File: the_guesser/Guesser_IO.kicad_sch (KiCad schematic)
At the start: 17 parts, among them J1 Screw_Terminal_01x06, J4 Screw_Terminal_01x06, J7 USB_C_Receptacle_USB2.0_16P, Q1 AS2312, Q2 AS2312, Q3 AS2312, Q4 AS2312, Q5 AS2312, Q6 AS2312, U13 TPD4S014DSQR, U60 FUSB307BMPX

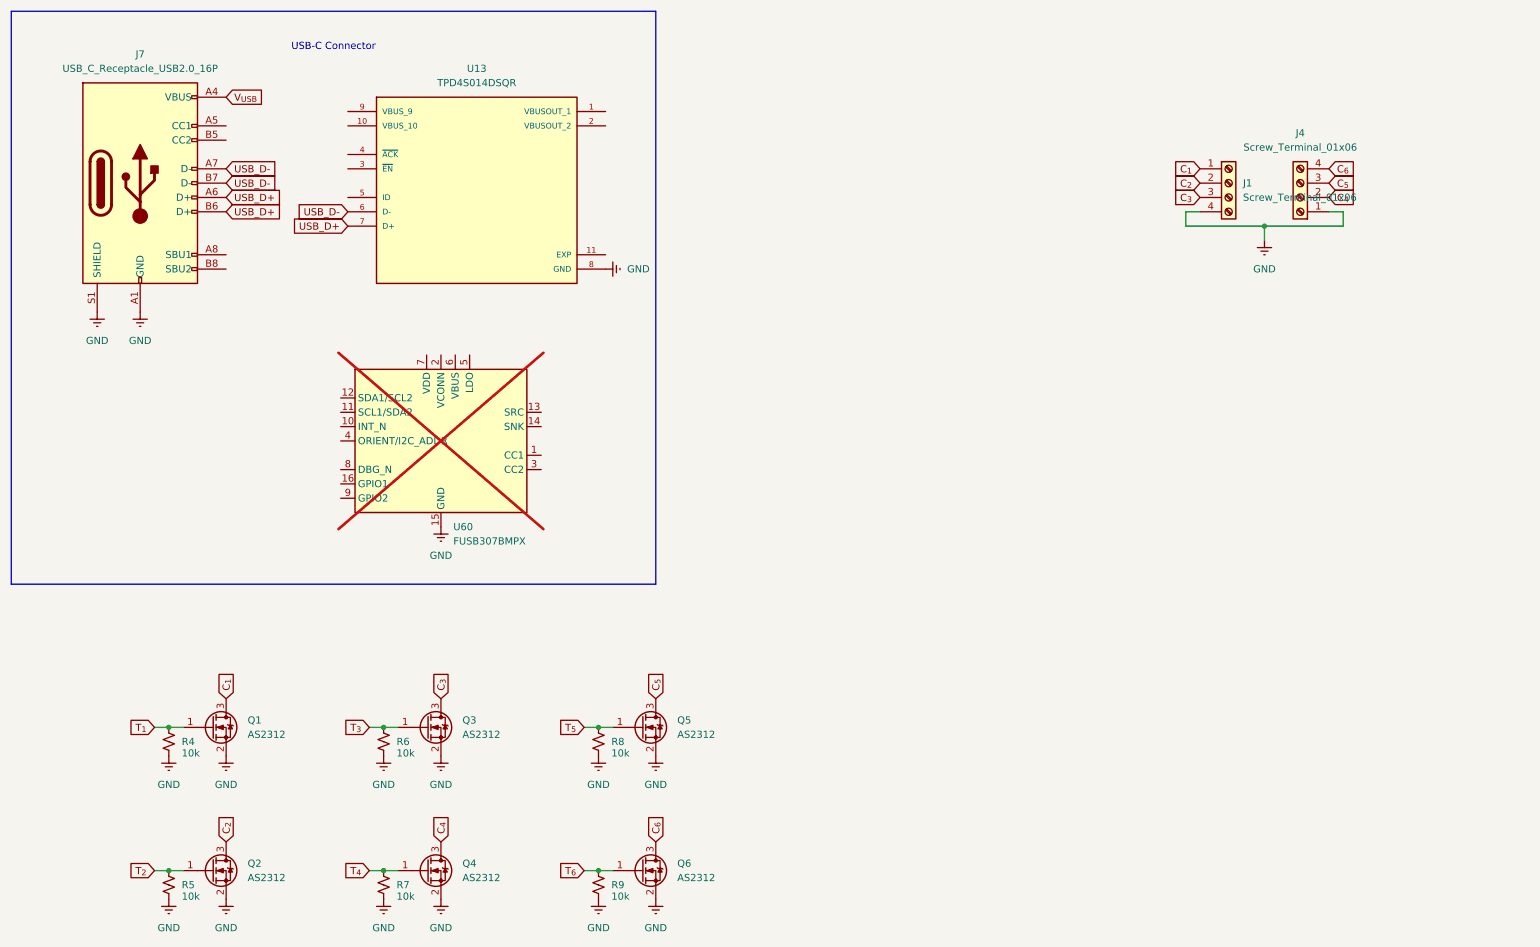
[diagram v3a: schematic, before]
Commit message: Finished routing Guesser
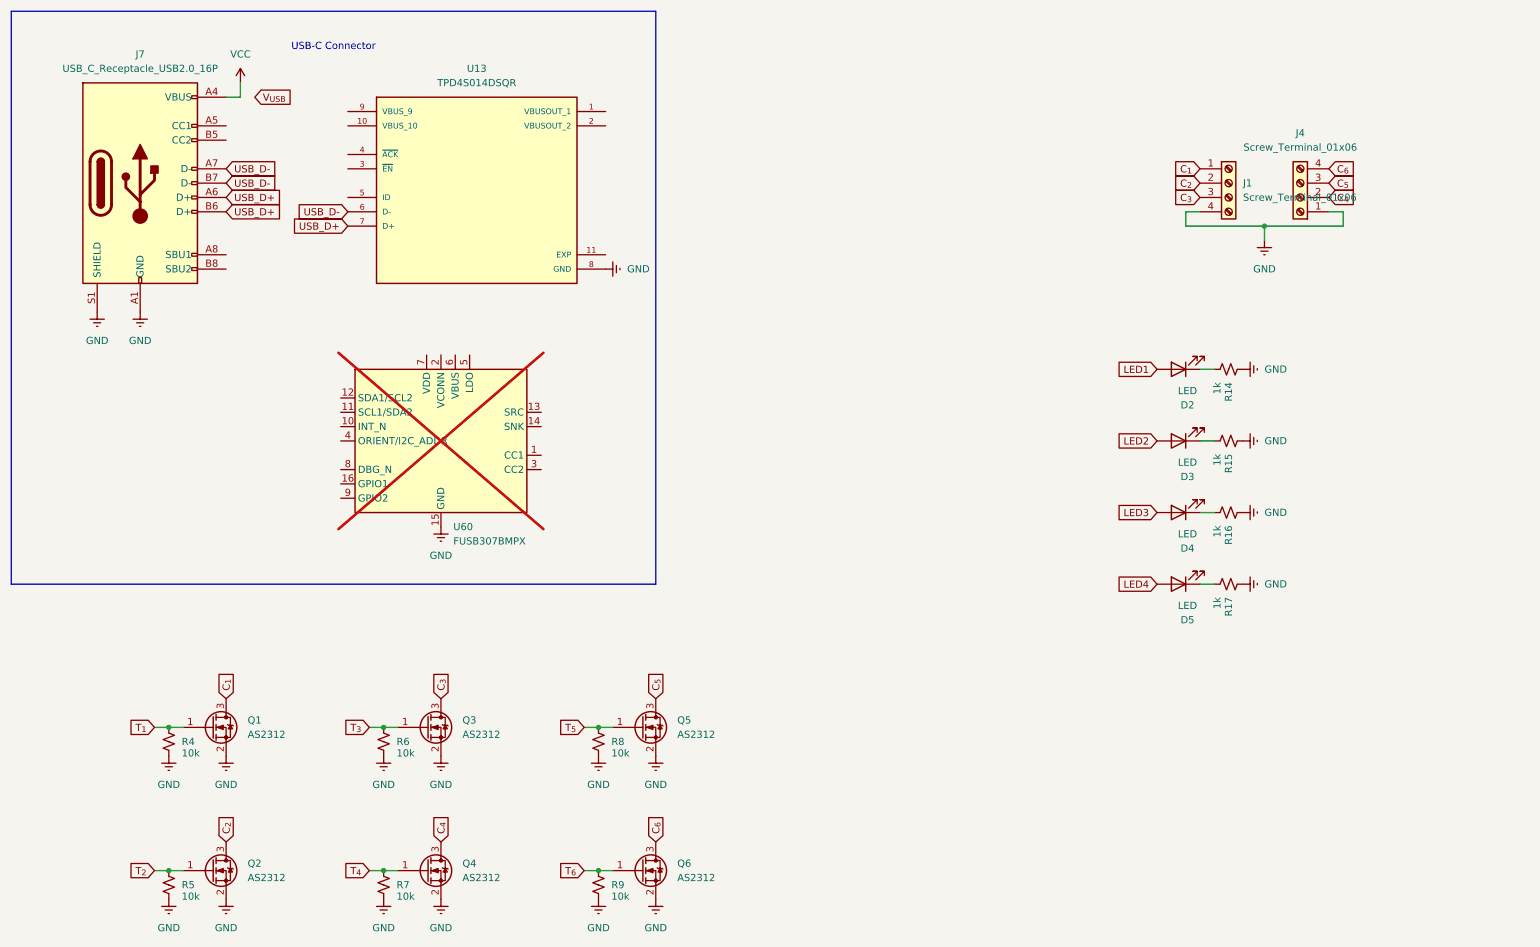
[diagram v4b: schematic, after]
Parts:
- added D2, D3, D4, D5: LED, LED_SMD:LED_0603_1608Metric, symbol Device:LED
- added R14, R15, R16, R17: 1k, Resistor_SMD:R_0603_1608Metric, symbol Device:R_Small_US
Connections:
- net GND: now also R14.1, R15.1, R16.1, R17.1
- net V_{USB}: no longer J7.A4 (VBUS), J7.A9 (VBUS), J7.B4 (VBUS), J7.B9 (VBUS)
- new net: D4.1 (K), R16.2
- new net: D3.1 (K), R15.2
- new net: D2.1 (K), R14.2
- new net: D5.1 (K), R17.2
- new net LED1: D2.2 (A)
- new net LED2: D3.2 (A)
- new net LED3: D4.2 (A)
- new net LED4: D5.2 (A)
- new net VCC: J7.A4 (VBUS), J7.A9 (VBUS), J7.B4 (VBUS), J7.B9 (VBUS)

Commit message: Started Timer Programmer
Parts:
- removed J7: USB_C_Receptacle_USB2.0_16P, Connector_USB:USB_C_Receptacle_GCT_USB4110, symbol Connector:USB_C_Receptacle_USB2.0_16P
- added J5: R41-B583A, locals_but_working_PLEASE:CONN_R41-B583A_MIT, symbol Connector:USB_C_Receptacle
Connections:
- net GND: now also J5.A1 (GND), J5.A12 (GND), J5.B1 (GND), J5.B12 (GND), J5.S1 (SHIELD)
- net USB_D+: now also J5.A6 (D+), J5.B6 (D+)
- net USB_D-: now also J5.A7 (D-), J5.B7 (D-)
- net VCC: now also J5.A4 (VBUS), J5.A9 (VBUS), J5.B4 (VBUS), J5.B9 (VBUS)
- no-connect marks 0 -> 8
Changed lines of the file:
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@@
 		(color 0 0 0 0)
 	)
+	(no_connect
+		(at 50.8 60.96)
+	)
+	(no_connect
+		(at 50.8 76.2)
+	)
+	(no_connect
+		(at 50.8 55.88)
+	)
+	(no_connect
+		(at 50.8 78.74)
+	)
+	(no_connect
+		(at 50.8 68.58)
+	)
+	(no_connect
+		(at 50.8 71.12)
+	)
+	(no_connect
+		(at 50.8 63.5)
+	)
+	(no_connect
+		(at 50.8 53.34)
+	)
 	(wire
 		(pts
@@
 		)
 	)
-	(global_label "V_{USB}"
-		(shape input)
-		(at 55.88 27.94 0)
-		(fields_autoplaced yes)
-		(effects
-			(font
-				(size 1.27 1.27)
-			)
-			(justify left)
-		)
-		(property "Intersheetrefs" "${INTERSHEET_REFS}"
-			(at 63.0526 27.94 0)
-			(effects
-				(font
-					(size 1.27 1.27)
-				)
-				(justify left)
-				(hide yes)
-			)
-		)
-	)
 	(global_label "C_{4}"
 		(shape input)
@@
 	(symbol
 		(lib_id "power:Earth")
-		(at 27.94 66.04 0)
+		(at 27.94 93.98 0)
 		(unit 1)
 		(exclude_from_sim no)
@@
 		(fields_autoplaced yes)
 		(property "Reference" "#PWR045"
-			(at 27.94 72.39 0)
+			(at 27.94 100.33 0)
 			(effects
 				(font
@@
 		)
 		(property "Value" "GND"
-			(at 27.94 71.12 0)
+			(at 27.94 99.06 0)
 			(effects
 				(font
@@
 		)
 		(property "Footprint" ""
-			(at 27.94 66.04 0)
+			(at 27.94 93.98 0)
 			(effects
 				(font
@@
 		)
 		(property "Datasheet" "~"
-			(at 27.94 66.04 0)
+			(at 27.94 93.98 0)
 			(effects
 				(font
@@
 		)
 		(property "Description" "Power symbol creates a global label with name \"Earth\""
-			(at 27.94 66.04 0)
+			(at 27.94 93.98 0)
 			(effects
 				(font
@@
 	)
 	(symbol
-		(lib_id "Connector:USB_C_Receptacle_USB2.0_16P")
-		(at 35.56 43.18 0)
-		(unit 1)
-		(exclude_from_sim no)
-		(in_bom yes)
-		(on_board yes)
-		(dnp no)
-		(fields_autoplaced yes)
-		(property "Reference" "J7"
-			(at 35.56 20.32 0)
-			(effects
-				(font
-					(size 1.27 1.27)
-				)
-			)
-		)
-		(property "Value" "USB_C_Receptacle_USB2.0_16P"
-			(at 35.56 22.86 0)
-			(effects
-				(font
-					(size 1.27 1.27)
-				)
-			)
-		)
-		(property "Footprint" "Connector_USB:USB_C_Receptacle_GCT_USB4110"
-			(at 39.37 43.18 0)
-			(effects
-				(font
-					(size 1.27 1.27)
-				)
-				(hide yes)
-			)
-		)
-		(property "Datasheet" "https://www.usb.org/sites/default/files/documents/usb_type-c.zip"
-			(at 39.37 43.18 0)
-			(effects
-				(font
-					(size 1.27 1.27)
-				)
-				(hide yes)
-			)
-		)
-		(property "Description" "USB 2.0-only 16P Type-C Receptacle connector"
-			(at 35.56 43.18 0)
-			(effects
-				(font
-					(size 1.27 1.27)
-				)
-				(hide yes)
-			)
-		)
-		(pin "B12"
-		)
-		(pin "A5"
-		)
-		(pin "B7"
-		)
-		(pin "A7"
-		)
-		(pin "B8"
-		)
-		(pin "A12"
-		)
-		(pin "S1"
-		)
-		(pin "B1"
-		)
-		(pin "B6"
-		)
-		(pin "B5"
-		)
-		(pin "A9"
-		)
-		(pin "A1"
-		)
-		(pin "A6"
-		)
-		(pin "A8"
-		)
-		(pin "A4"
-		)
-		(pin "B4"
-		)
-		(pin "B9"
-		)
-		(instances
-			(project "the_guesser"
-				(path "/473e3a2e-6c5e-4995-af4a-e4bf1449cab0/0bcaec57-f6d5-41f0-b678-342e153337b7"
-					(reference "J7")
-					(unit 1)
-				)
-			)
-		)
-	)
-	(symbol
 		(lib_id "Connector:Screw_Terminal_01x04")
 		(at 228.6 43.18 0)
@@
 	)
 	(symbol
+		(lib_id "Connector:USB_C_Receptacle")
+		(at 35.56 53.34 0)
+		(unit 1)
+		(exclude_from_sim no)
+		(in_bom yes)
+		(on_board yes)
+		(dnp no)
+		(fields_autoplaced yes)
+		(property "Reference" "J5"
+			(at 35.56 20.32 0)
+			(effects
+				(font
+					(size 1.27 1.27)
+				)
+			)
+		)
+		(property "Value" "R41-B583A"
+			(at 35.56 22.86 0)
+			(effects
+				(font
+					(size 1.27 1.27)
+				)
+			)
+		)
+		(property "Footprint" "locals_but_working_PLEASE:CONN_R41-B583A_MIT"
+			(at 39.37 53.34 0)
+			(effects
+				(font
+					(size 1.27 1.27)
+				)
+				(hide yes)
+			)
+		)
+		(property "Datasheet" "https://www.usb.org/sites/default/files/documents/usb_type-c.zip"
+			(at 39.37 53.34 0)
+			(effects
+				(font
+					(size 1.27 1.27)
+				)
+				(hide yes)
+			)
+		)
+		(property "Description" "USB Full-Featured Type-C Receptacle connector"
+			(at 35.56 53.34 0)
+			(effects
+				(font
+					(size 1.27 1.27)
+				)
+				(hide yes)
+			)
+		)
+		(property "DKPN" "2508-R41-B583ACT-ND"
+			(at 35.56 53.34 0)
+			(effects
+				(font
+					(size 1.27 1.27)
+				)
+				(hide yes)
+			)
+		)
+		(pin "A5"
+		)
+		(pin "B8"
+		)
+		(pin "A6"
+		)
+		(pin "A4"
+		)
+		(pin "S1"
+		)
+		(pin "B10"
+		)
+		(pin "A1"
+		)
+		(pin "A7"
+		)
+		(pin "B6"
+		)
+		(pin "A3"
+		)
+		(pin "A9"
+		)
+		(pin "B3"
+		)
+		(pin "A2"
+		)
+		(pin "B9"
+		)
+		(pin "A12"
+		)
+		(pin "B11"
+		)
+		(pin "B12"
+		)
+		(pin "A8"
+		)
+		(pin "B1"
+		)
+		(pin "A11"
+		)
+		(pin "B2"
+		)
+		(pin "B7"
+		)
+		(pin "B4"
+		)
+		(pin "A10"
+		)
+		(pin "B5"
+		)
+		(instances
+			(project "the_guesser"
+				(path "/473e3a2e-6c5e-4995-af4a-e4bf1449cab0/0bcaec57-f6d5-41f0-b678-342e153337b7"
+					(reference "J5")
+					(unit 1)
+				)
+			)
+		)
+	)
+	(symbol
 		(lib_id "Device:LED")
 		(at 219.71 114.3 180)
@@
 	(symbol
 		(lib_id "power:Earth")
-		(at 35.56 66.04 0)
+		(at 35.56 93.98 0)
 		(unit 1)
 		(exclude_from_sim no)
@@
 		(fields_autoplaced yes)
 		(property "Reference" "#PWR046"
-			(at 35.56 72.39 0)
+			(at 35.56 100.33 0)
 			(effects
 				(font
@@
 		)
 		(property "Value" "GND"
-			(at 35.56 71.12 0)
+			(at 35.56 99.06 0)
 			(effects
 				(font
@@
 		)
 		(property "Footprint" ""
-			(at 35.56 66.04 0)
+			(at 35.56 93.98 0)
 			(effects
 				(font
@@
 		)
 		(property "Datasheet" "~"
-			(at 35.56 66.04 0)
+			(at 35.56 93.98 0)
 			(effects
 				(font
@@
 		)
 		(property "Description" "Power symbol creates a global label with name \"Earth\""
-			(at 35.56 66.04 0)
+			(at 35.56 93.98 0)
 			(effects
 				(font

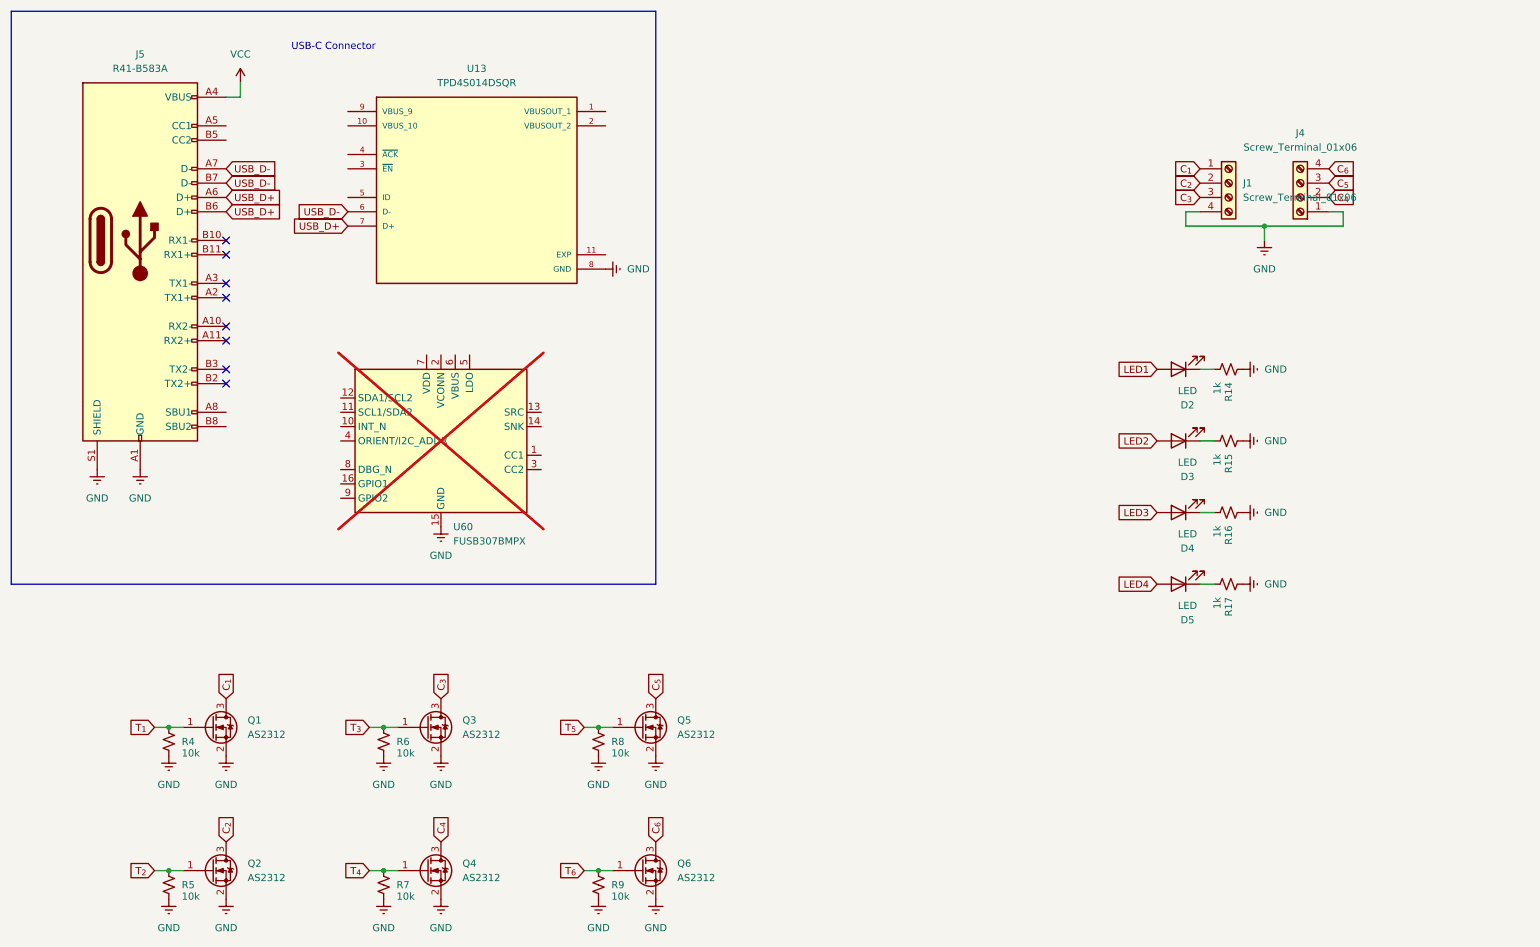
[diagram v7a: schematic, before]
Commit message: Updated Guesser USB and GPS
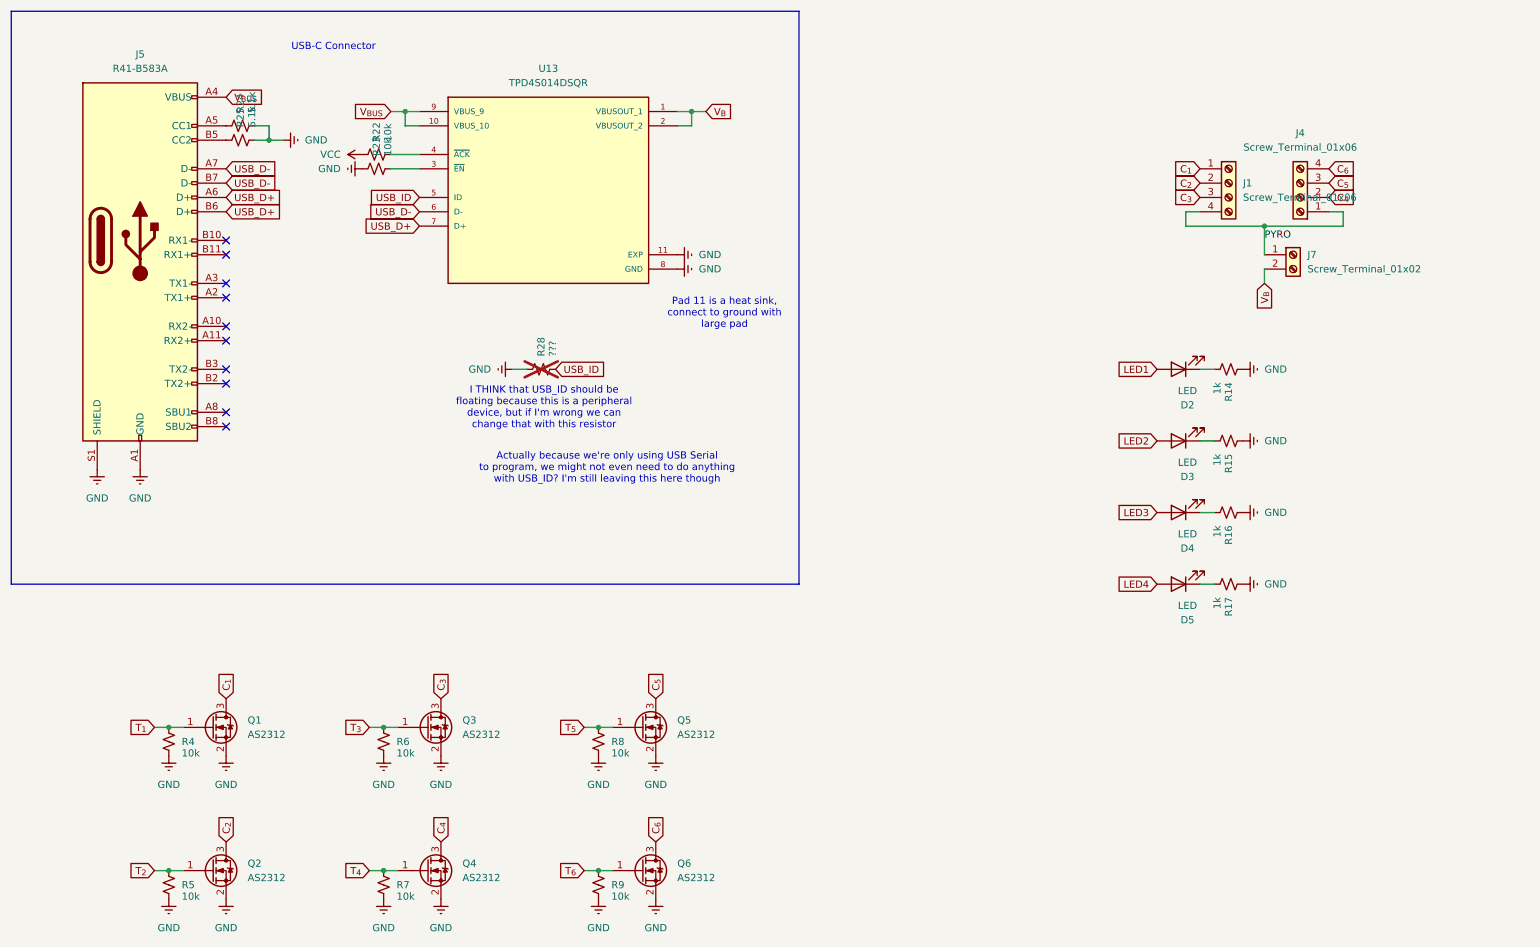
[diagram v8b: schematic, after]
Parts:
- removed U60: FUSB307BMPX, Package_DFN_QFN:WQFN-16-1EP_3x3mm_P0.5mm_EP1.75x1.75mm, symbol Interface_USB:FUSB307BMPX
- added J7: Screw_Terminal_01x02, TerminalBlock_Phoenix:TerminalBlock_Phoenix_MPT-0,5-2-2.54_1x02_P2.54mm_Horizontal, symbol Connector:Screw_Terminal_01x02
- added R22, R23: 10k, Resistor_SMD:R_0603_1608Metric, symbol Device:R_Small_US
- added R24, R25: 5.1k, Resistor_SMD:R_0603_1608Metric, symbol Device:R_Small_US
- added R28: ???, Resistor_SMD:R_0603_1608Metric, symbol Device:R_Small_US
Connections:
- net GND: now also U13.11 (EXP), R23.1, R24.2, R25.2, R28.1; no longer J1.4 (Pin_4), J4.1 (Pin_1)
- net VCC: now also R22.1; no longer J5.A4 (VBUS), J5.A9 (VBUS), J5.B4 (VBUS), J5.B9 (VBUS)
- net V_{B}: now reaches U13.1 (VBUSOUT_1)
- net V_{B}: now also U13.2 (VBUSOUT_2), J7.2 (Pin_2)
- net V_{BUS}: now reaches U13.10 (VBUS_10)
- net V_{BUS}: now also J5.A4 (VBUS), J5.A9 (VBUS), J5.B4 (VBUS), J5.B9 (VBUS), U13.9 (VBUS_9)
- net at U13.3 (~{EN}): now also R23.2
- net at U13.4 (~{ACK}): now also R22.2
- net USB_ID: now reaches U13.5 (ID)
- net USB_ID: now also R28.2
- net at J5.A5 (CC1): now also R24.1
- net at J5.B5 (CC2): now also R25.1
- new net PYRO: J1.4 (Pin_4), J4.1 (Pin_1), J7.1 (Pin_1)
- no-connect marks 8 -> 10
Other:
- note added: "Actually because we're only using USB Serial to program, we might not even need to do anything with USB_ID? I'm still leaving this here though"
- note added: "I THINK that USB_ID should be floating because this is a peripheral device, but if I'm wrong we can change that with this resistor"
- note added: "Pad 11 is a heat sink, connect to ground with large pad"
- moved on the sheet: U13
